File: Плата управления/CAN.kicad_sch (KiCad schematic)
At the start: 10 parts

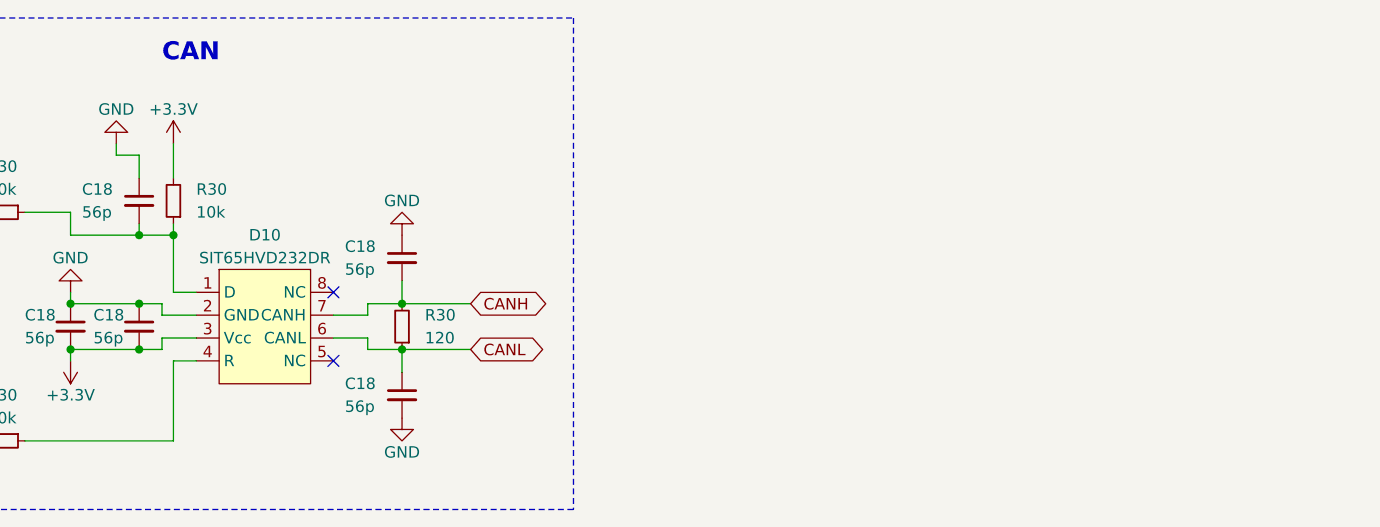
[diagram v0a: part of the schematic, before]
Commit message: Изменил контур под новую крышку
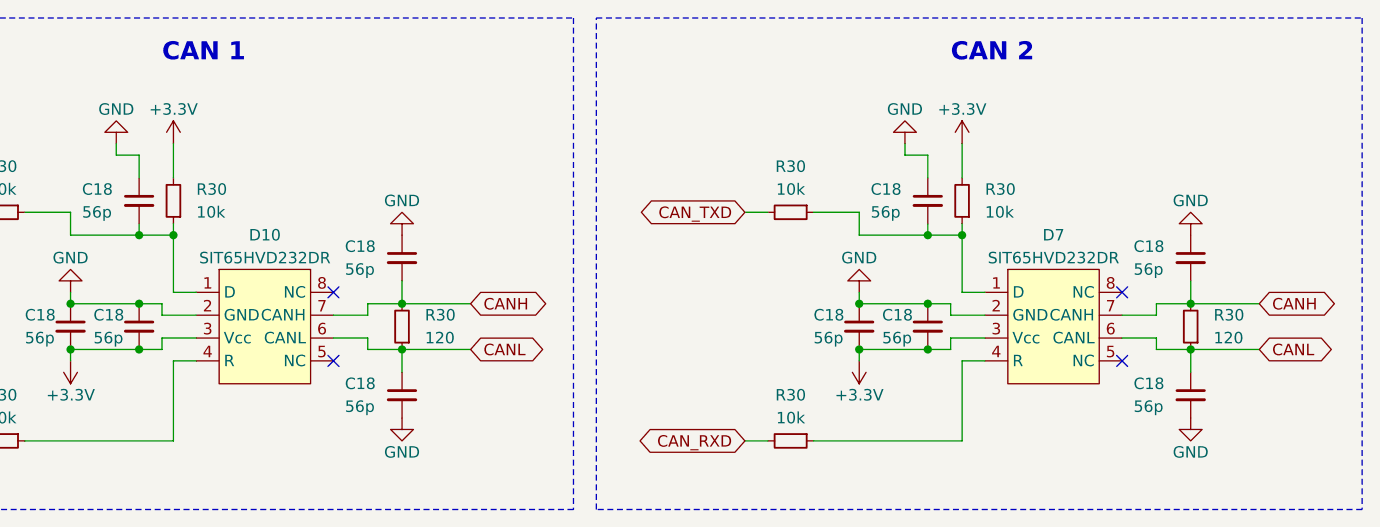
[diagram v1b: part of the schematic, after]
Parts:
- added C18 (x5): 56p, Capacitor_SMD:C_0603_1608Metric_Pad1.08x0.95mm_HandSolder, symbol Device:C_Small
- added D7: SIT65HVD232DR, Package_SO:SOIC-8_3.9x4.9mm_P1.27mm, symbol CAN_My:SIT65HVD232DR
- added R30 (x3): 10k, Resistor_SMD:R_0603_1608Metric_Pad0.98x0.95mm_HandSolder, symbol Device:R_Small
- added R30: 120, Resistor_SMD:R_0603_1608Metric_Pad0.98x0.95mm_HandSolder, symbol Device:R_Small
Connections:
- net +3.3V: now also C18.2, C18.2, D7.3 (Vcc), R30.2
- net CANH: now also C18.2, D7.7 (CANH), R30.2
- net CANL: now also C18.1, D7.6 (CANL), R30.1
- net CAN_RXD: now also R30.2
- net CAN_TXD: now also R30.2
- net GND: now also C18.1, C18.1, C18.1, C18.1, C18.2, D7.2 (GND)
- new net: C18.2, D7.1 (D), R30.1, R30.1
- new net: D7.4 (R), R30.1
- no-connect marks 2 -> 4
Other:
- note added: "CAN 1"
- note added: "CAN 2"
- note removed: "CAN"

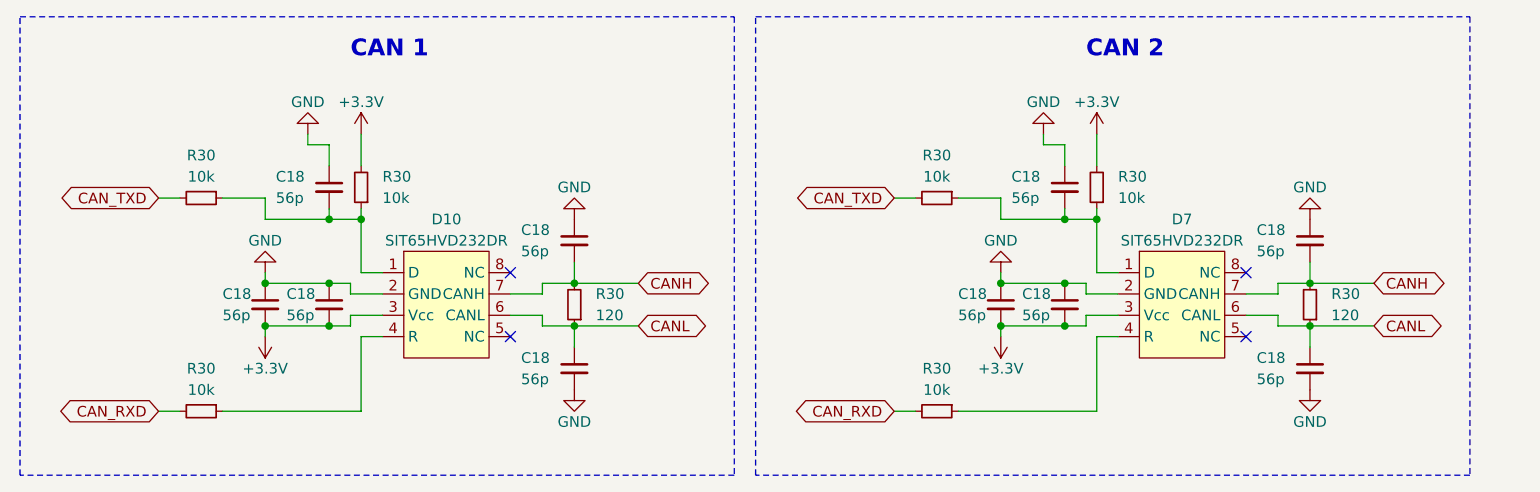
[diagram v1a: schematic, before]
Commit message: Добавил разъёмы под интерфейсы
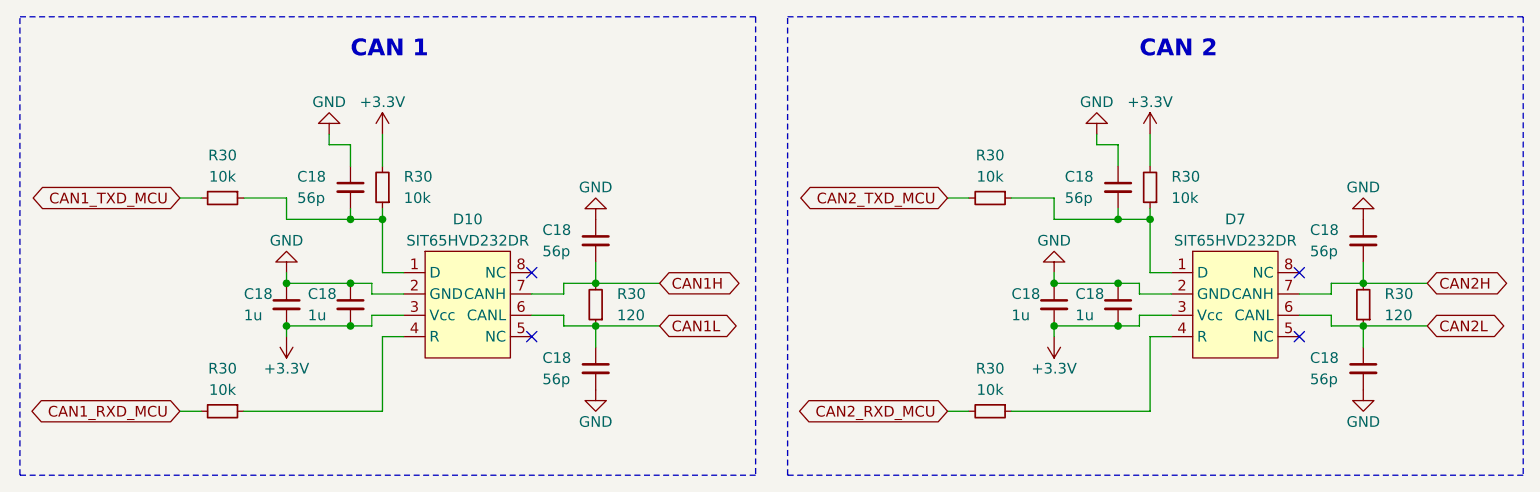
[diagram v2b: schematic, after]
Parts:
- C18: value 56p -> 1u
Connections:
- net CANH renamed CAN1H
- net CAN1H: no longer C18.2, D7.7 (CANH), R30.2
- net CANL renamed CAN1L
- net CAN1L: no longer C18.1, D7.6 (CANL), R30.1
- net CAN_RXD renamed CAN1_RXD_MCU
- net CAN1_RXD_MCU: no longer R30.2
- net CAN_TXD renamed CAN1_TXD_MCU
- net CAN1_TXD_MCU: no longer R30.2
- new net CAN2H: C18.2, D7.7 (CANH), R30.2
- new net CAN2L: C18.1, D7.6 (CANL), R30.1
- new net CAN2_RXD_MCU: R30.2
- new net CAN2_TXD_MCU: R30.2
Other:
- moved on the sheet: C18, D10, D7, R30

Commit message: Новый контур платы
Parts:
- removed R30 (x2): 10k, Resistor_SMD:R_0603_1608Metric_Pad0.98x0.95mm_HandSolder, symbol Device:R_Small
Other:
- moved on the sheet: C18

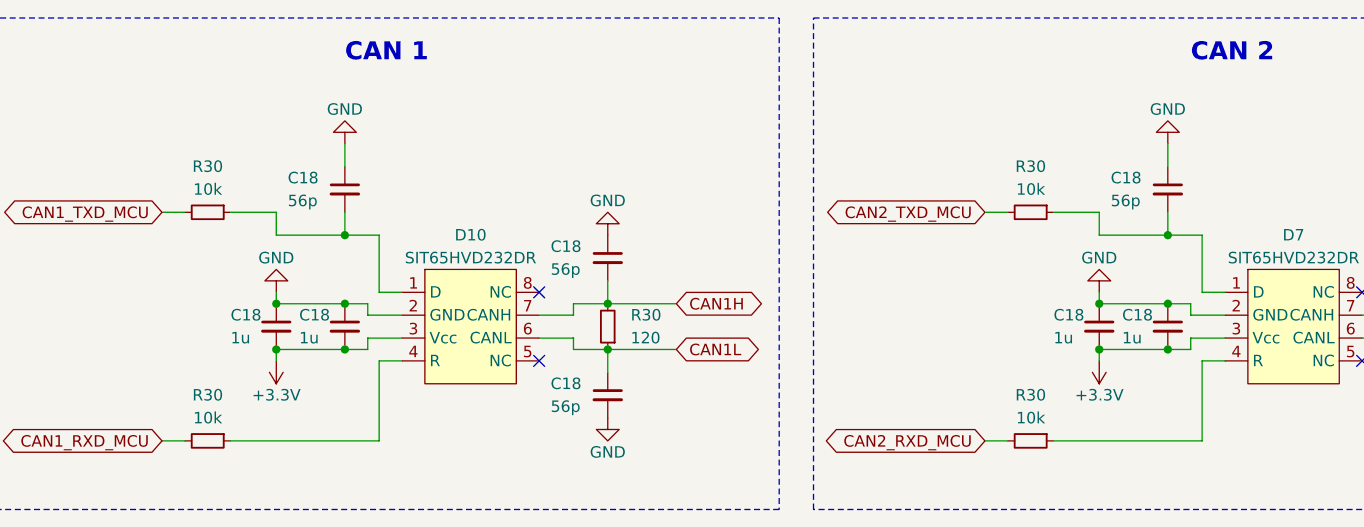
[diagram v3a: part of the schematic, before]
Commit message: Заменил разъём под силовую плату
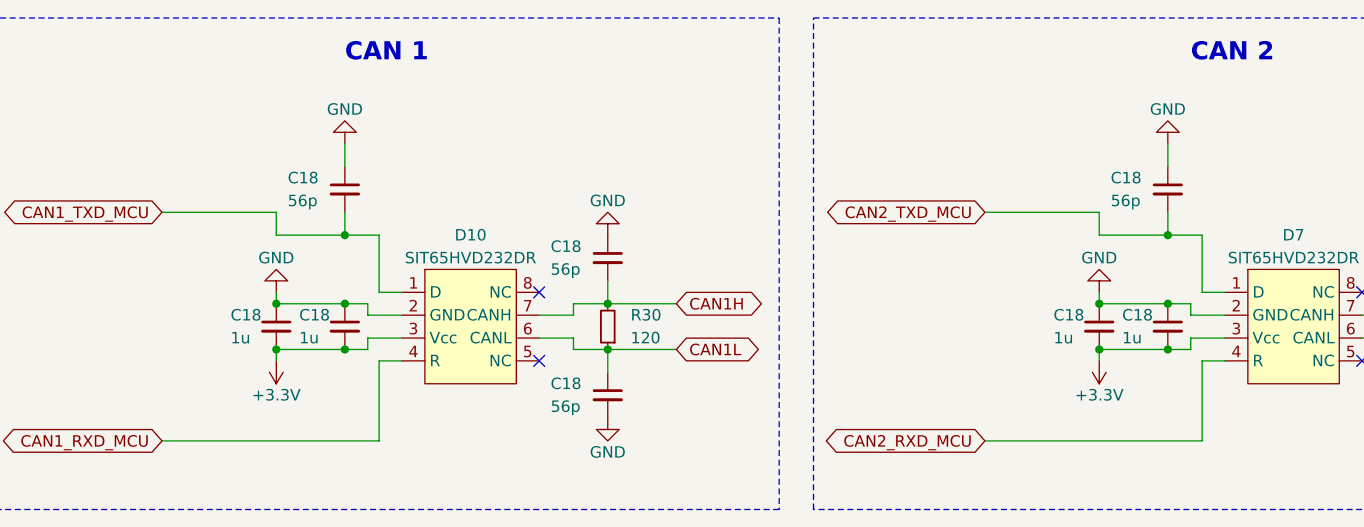
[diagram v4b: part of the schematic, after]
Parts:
- removed R30 (x4): 10k, Resistor_SMD:R_0603_1608Metric_Pad0.98x0.95mm_HandSolder, symbol Device:R_Small
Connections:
- net CAN1_RXD_MCU: now also D10.4 (R)
- net CAN1_TXD_MCU: now also C18.2, D10.1 (D)
- net CAN2_RXD_MCU: now also D7.4 (R)
- net CAN2_TXD_MCU: now also C18.2, D7.1 (D)
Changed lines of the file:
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@@
     (stroke (width 0) (type default))
   )
-  (wire (pts (xy 34.29 36.83) (xy 36.83 36.83))
-    (stroke (width 0) (type default))
-  )
-  (wire (pts (xy 34.29 62.23) (xy 36.83 62.23))
+  (wire (pts (xy 34.29 62.23) (xy 58.42 62.23))
     (stroke (width 0) (type default))
   )
@@
     (stroke (width 0) (type default))
   )
-  (wire (pts (xy 41.91 36.83) (xy 46.99 36.83))
+  (wire (pts (xy 34.29 36.83) (xy 46.99 36.83))
     (stroke (width 0) (type default))
   )
@@
     (stroke (width 0) (type default))
   )
-  (wire (pts (xy 125.73 36.83) (xy 128.27 36.83))
-    (stroke (width 0) (type default))
-  )
-  (wire (pts (xy 41.91 62.23) (xy 58.42 62.23))
-    (stroke (width 0) (type default))
-  )
   (wire (pts (xy 57.15 50.8) (xy 60.96 50.8))
     (stroke (width 0) (type default))
@@
     (stroke (width 0) (type default))
   )
-  (wire (pts (xy 133.35 36.83) (xy 138.43 36.83))
+  (wire (pts (xy 125.73 36.83) (xy 138.43 36.83))
     (stroke (width 0) (type default))
   )
@@
     (stroke (width 0) (type default))
   )
-  (wire (pts (xy 125.73 62.23) (xy 128.27 62.23))
-    (stroke (width 0) (type default))
-  )
   (wire (pts (xy 46.99 36.83) (xy 46.99 39.37))
     (stroke (width 0) (type default))
@@
     (stroke (width 0) (type default))
   )
-  (wire (pts (xy 133.35 62.23) (xy 149.86 62.23))
+  (wire (pts (xy 125.73 62.23) (xy 149.86 62.23))
     (stroke (width 0) (type default))
   )
@@
     )
   )
-  (symbol (lib_id "Device:R_Small") (at 39.37 62.23 270) (unit 1)
-    (in_bom yes) (on_board yes) (dnp no) (fields_autoplaced)
-    (property "Reference" "R30" (at 39.37 57.15 90)
-      (effects (font (size 1.27 1.27)))
-    )
-    (property "Value" "10k" (at 39.37 59.69 90)
-      (effects (font (size 1.27 1.27)))
-    )
-    (property "Footprint" "Resistor_SMD:R_0603_1608Metric_Pad0.98x0.95mm_HandSolder" (at 39.37 62.23 0)
-      (effects (font (size 1.27 1.27)) hide)
-    )
-    (property "Datasheet" "~" (at 39.37 62.23 0)
-      (effects (font (size 1.27 1.27)) hide)
-    )
-    (pin "1")
-    (pin "2")
-    (instances
-      (project "Плата управления"
-        (path "/75f4c67c-bbde-4446-8f82-67797a1b269f/d6b8b9ce-300b-4d22-9d4c-9182eba581b1"
-          (reference "R30") (unit 1)
-        )
-        (path "/75f4c67c-bbde-4446-8f82-67797a1b269f/c91ff3ec-ad20-4326-acd4-2c9dea437172"
-          (reference "R20") (unit 1)
-        )
-        (path "/75f4c67c-bbde-4446-8f82-67797a1b269f/9fed4cc9-7de2-4454-9cda-928fae308673"
-          (reference "R33") (unit 1)
-        )
-        (path "/75f4c67c-bbde-4446-8f82-67797a1b269f/bbae964f-aef3-47b6-89c5-594b5cc7787c"
-          (reference "R15") (unit 1)
-        )
-        (path "/75f4c67c-bbde-4446-8f82-67797a1b269f/c4a77b60-6f80-4c82-a865-c1484ac69908"
-          (reference "R15") (unit 1)
-        )
-      )
-      (project "Силовая плата"
-        (path "/96c6fc92-8ec6-44f7-b0dc-9ad8f1acea09/1efb5faf-bb82-4ac6-a144-d6576b4720aa"
-          (reference "R2") (unit 1)
-        )
-      )
-    )
-  )
   (symbol (lib_id "Device:C_Small") (at 146.05 34.29 0) (unit 1)
     (in_bom yes) (on_board yes) (dnp no)
@@
         (path "/96c6fc92-8ec6-44f7-b0dc-9ad8f1acea09/a27b443f-c036-4fd6-934c-6ea912709de0"
           (reference "#PWR025") (unit 1)
-        )
-      )
-    )
-  )
-  (symbol (lib_id "Device:R_Small") (at 130.81 36.83 270) (unit 1)
-    (in_bom yes) (on_board yes) (dnp no) (fields_autoplaced)
-    (property "Reference" "R30" (at 130.81 31.75 90)
-      (effects (font (size 1.27 1.27)))
-    )
-    (property "Value" "10k" (at 130.81 34.29 90)
-      (effects (font (size 1.27 1.27)))
-    )
-    (property "Footprint" "Resistor_SMD:R_0603_1608Metric_Pad0.98x0.95mm_HandSolder" (at 130.81 36.83 0)
-      (effects (font (size 1.27 1.27)) hide)
-    )
-    (property "Datasheet" "~" (at 130.81 36.83 0)
-      (effects (font (size 1.27 1.27)) hide)
-    )
-    (pin "1")
-    (pin "2")
-    (instances
-      (project "Плата управления"
-        (path "/75f4c67c-bbde-4446-8f82-67797a1b269f/d6b8b9ce-300b-4d22-9d4c-9182eba581b1"
-          (reference "R30") (unit 1)
-        )
-        (path "/75f4c67c-bbde-4446-8f82-67797a1b269f/c91ff3ec-ad20-4326-acd4-2c9dea437172"
-          (reference "R20") (unit 1)
-        )
-        (path "/75f4c67c-bbde-4446-8f82-67797a1b269f/9fed4cc9-7de2-4454-9cda-928fae308673"
-          (reference "R27") (unit 1)
-        )
-        (path "/75f4c67c-bbde-4446-8f82-67797a1b269f/bbae964f-aef3-47b6-89c5-594b5cc7787c"
-          (reference "R14") (unit 1)
-        )
-        (path "/75f4c67c-bbde-4446-8f82-67797a1b269f/c4a77b60-6f80-4c82-a865-c1484ac69908"
-          (reference "R14") (unit 1)
-        )
-      )
-      (project "Силовая плата"
-        (path "/96c6fc92-8ec6-44f7-b0dc-9ad8f1acea09/1efb5faf-bb82-4ac6-a144-d6576b4720aa"
-          (reference "R2") (unit 1)
         )
       )
@@
     )
   )
-  (symbol (lib_id "Device:R_Small") (at 130.81 62.23 270) (unit 1)
-    (in_bom yes) (on_board yes) (dnp no) (fields_autoplaced)
-    (property "Reference" "R30" (at 130.81 57.15 90)
-      (effects (font (size 1.27 1.27)))
-    )
-    (property "Value" "10k" (at 130.81 59.69 90)
-      (effects (font (size 1.27 1.27)))
-    )
-    (property "Footprint" "Resistor_SMD:R_0603_1608Metric_Pad0.98x0.95mm_HandSolder" (at 130.81 62.23 0)
-      (effects (font (size 1.27 1.27)) hide)
-    )
-    (property "Datasheet" "~" (at 130.81 62.23 0)
-      (effects (font (size 1.27 1.27)) hide)
-    )
-    (pin "1")
-    (pin "2")
-    (instances
-      (project "Плата управления"
-        (path "/75f4c67c-bbde-4446-8f82-67797a1b269f/d6b8b9ce-300b-4d22-9d4c-9182eba581b1"
-          (reference "R30") (unit 1)
-        )
-        (path "/75f4c67c-bbde-4446-8f82-67797a1b269f/c91ff3ec-ad20-4326-acd4-2c9dea437172"
-          (reference "R20") (unit 1)
-        )
-        (path "/75f4c67c-bbde-4446-8f82-67797a1b269f/9fed4cc9-7de2-4454-9cda-928fae308673"
-          (reference "R28") (unit 1)
-        )
-        (path "/75f4c67c-bbde-4446-8f82-67797a1b269f/bbae964f-aef3-47b6-89c5-594b5cc7787c"
-          (reference "R15") (unit 1)
-        )
-        (path "/75f4c67c-bbde-4446-8f82-67797a1b269f/c4a77b60-6f80-4c82-a865-c1484ac69908"
-          (reference "R15") (unit 1)
-        )
-      )
-      (project "Силовая плата"
-        (path "/96c6fc92-8ec6-44f7-b0dc-9ad8f1acea09/1efb5faf-bb82-4ac6-a144-d6576b4720aa"
-          (reference "R2") (unit 1)
-        )
-      )
-    )
-  )
   (symbol (lib_id "Device:C_Small") (at 54.61 49.53 0) (unit 1)
     (in_bom yes) (on_board yes) (dnp no)
@@
         )
       )
-    )
-  )
-  (symbol (lib_id "Device:R_Small") (at 39.37 36.83 270) (unit 1)
-    (in_bom yes) (on_board yes) (dnp no) (fields_autoplaced)
-    (property "Reference" "R30" (at 39.37 31.75 90)
-      (effects (font (size 1.27 1.27)))
-    )
-    (property "Value" "10k" (at 39.37 34.29 90)
-      (effects (font (size 1.27 1.27)))
-    )
-    (property "Footprint" "Resistor_SMD:R_0603_1608Metric_Pad0.98x0.95mm_HandSolder" (at 39.37 36.83 0)
-      (effects (font (size 1.27 1.27)) hide)
-    )
-    (property "Datasheet" "~" (at 39.37 36.83 0)
-      (effects (font (size 1.27 1.27)) hide)
-    )
-    (pin "1")
-    (pin "2")
-    (instances
-      (project "Плата управления"
-        (path "/75f4c67c-bbde-4446-8f82-67797a1b269f/d6b8b9ce-300b-4d22-9d4c-9182eba581b1"
-          (reference "R30") (unit 1)
-        )
-        (path "/75f4c67c-bbde-4446-8f82-67797a1b269f/c91ff3ec-ad20-4326-acd4-2c9dea437172"
-          (reference "R20") (unit 1)
-        )
-        (path "/75f4c67c-bbde-4446-8f82-67797a1b269f/9fed4cc9-7de2-4454-9cda-928fae308673"
-          (reference "R32") (unit 1)
-        )
-        (path "/75f4c67c-bbde-4446-8f82-67797a1b269f/bbae964f-aef3-47b6-89c5-594b5cc7787c"
-          (reference "R14") (unit 1)
-        )
-        (path "/75f4c67c-bbde-4446-8f82-67797a1b269f/c4a77b60-6f80-4c82-a865-c1484ac69908"
-          (reference "R14") (unit 1)
-        )
-      )
-      (project "Силовая плата"
-        (path "/96c6fc92-8ec6-44f7-b0dc-9ad8f1acea09/1efb5faf-bb82-4ac6-a144-d6576b4720aa"
-          (reference "R2") (unit 1)
-        )
-      )

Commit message: Редактировал схему
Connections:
- net CAN1H: now also C18.2, D7.7 (CANH), R30.2; no longer C18.2, D10.7 (CANH), R30.2
- net CAN1L: now also C18.1, D7.6 (CANL), R30.1; no longer C18.1, D10.6 (CANL), R30.1
- net CAN1_RXD_MCU: now also D7.4 (R); no longer D10.4 (R)
- net CAN1_TXD_MCU: now also C18.2, D7.1 (D); no longer C18.2, D10.1 (D)
- net CAN2H: now also C18.2, D10.7 (CANH), R30.2; no longer C18.2, D7.7 (CANH), R30.2
- net CAN2L: now also C18.1, D10.6 (CANL), R30.1; no longer C18.1, D7.6 (CANL), R30.1
- net CAN2_RXD_MCU: now also D10.4 (R); no longer D7.4 (R)
- net CAN2_TXD_MCU: now also C18.2, D10.1 (D); no longer C18.2, D7.1 (D)
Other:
- moved on the sheet: C18, D10, D7, R30

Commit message: Собираю документацию
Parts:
- added D8, D9: PESD2CAN, Package_TO_SOT_SMD:SOT-23, symbol Power_Protection:NUP2105L
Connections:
- net CAN1H: now also D9.1 (K)
- net CAN1L: now also D9.2 (K)
- net CAN2H: now also D8.1 (K)
- net CAN2L: now also D8.2 (K)
- net GND: now also D8.3 (A), D9.3 (A)
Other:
- moved on the sheet: C18, D10, D7, R30

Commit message: Добавил документы
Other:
- moved on the sheet: C18, D10, D7, D8, D9, R30

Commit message: Добавил все документы
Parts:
- renumbered D9 to D11, D8 to D12, D7 to D9
